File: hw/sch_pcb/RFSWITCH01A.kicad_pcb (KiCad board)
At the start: 2 copper layers, 40.1 x 40.1 mm, 43 parts, among them J1 HEADER_2x03_PARALLEL, J10 HEADER_2x01_PARALLEL, J2 SMA, J3 SMA, J4 HEADER_2x01_PARALLEL, J5 HEADER_2x01_PARALLEL, J6 HEADER_2x01_PARALLEL, J7 SMA, J8 SMA, J9 HEADER_2x01_PARALLEL, M1 HOLE, M2 HOLE, M3 HOLE, M4 HOLE, U1 TPS22945DCKR, U2 PE4259, U3 SPF5189Z, U4 PE4259

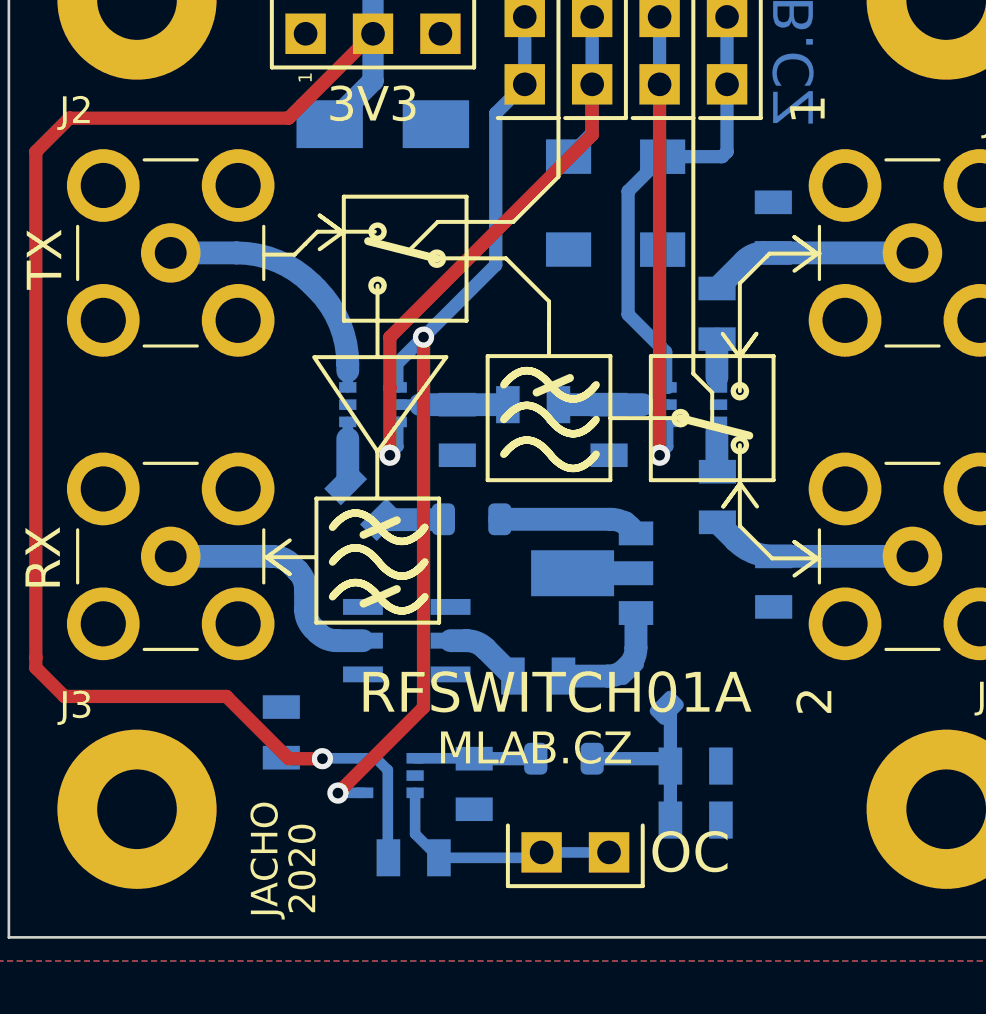
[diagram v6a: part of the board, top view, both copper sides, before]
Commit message: Diode, via, 3D model
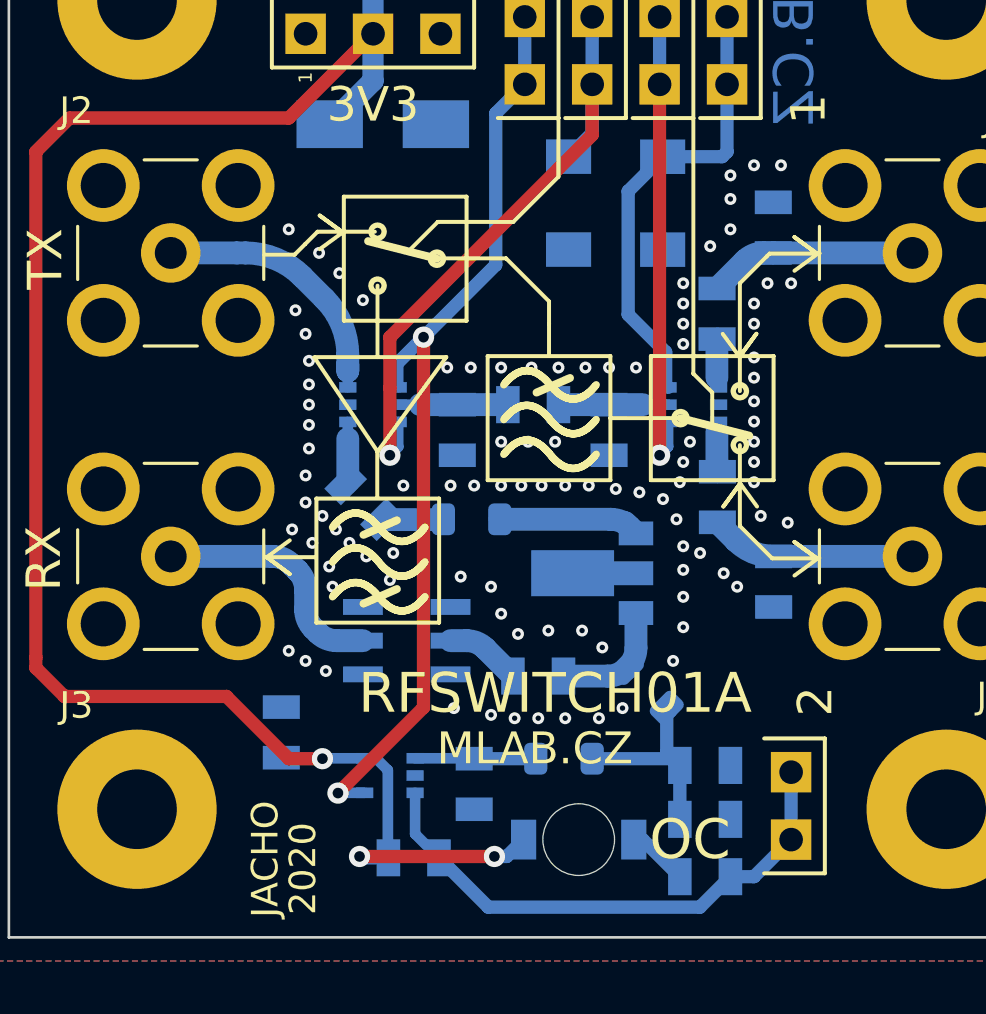
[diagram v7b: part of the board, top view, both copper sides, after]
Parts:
- added D4: RED, Mlab_D:LED_1206, B.Cu at (21.7, -3.94)
- added R6: 330R, Mlab_R:SMD-0805, B.Cu at (26.5, -2.54)
- moved J6 8.31 mm to (29.7, -5.21), turned to 90 degrees
- moved C4 0.36 mm to (26.5, -6.73)
- moved C3 0.36 mm to (26.5, -4.70)
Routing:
- net Net-(J6-Pad1): track 9.31 -> 21.0 mm
- net +3V3: track 74.8 -> 82.3 mm, vias 3 -> 5
- net Net-(D4-Pad1): track 0.00 -> 2.31 mm
- net Net-(C3-Pad1): track 7.35 -> 8.01 mm
- net GND: vias 0 -> 97

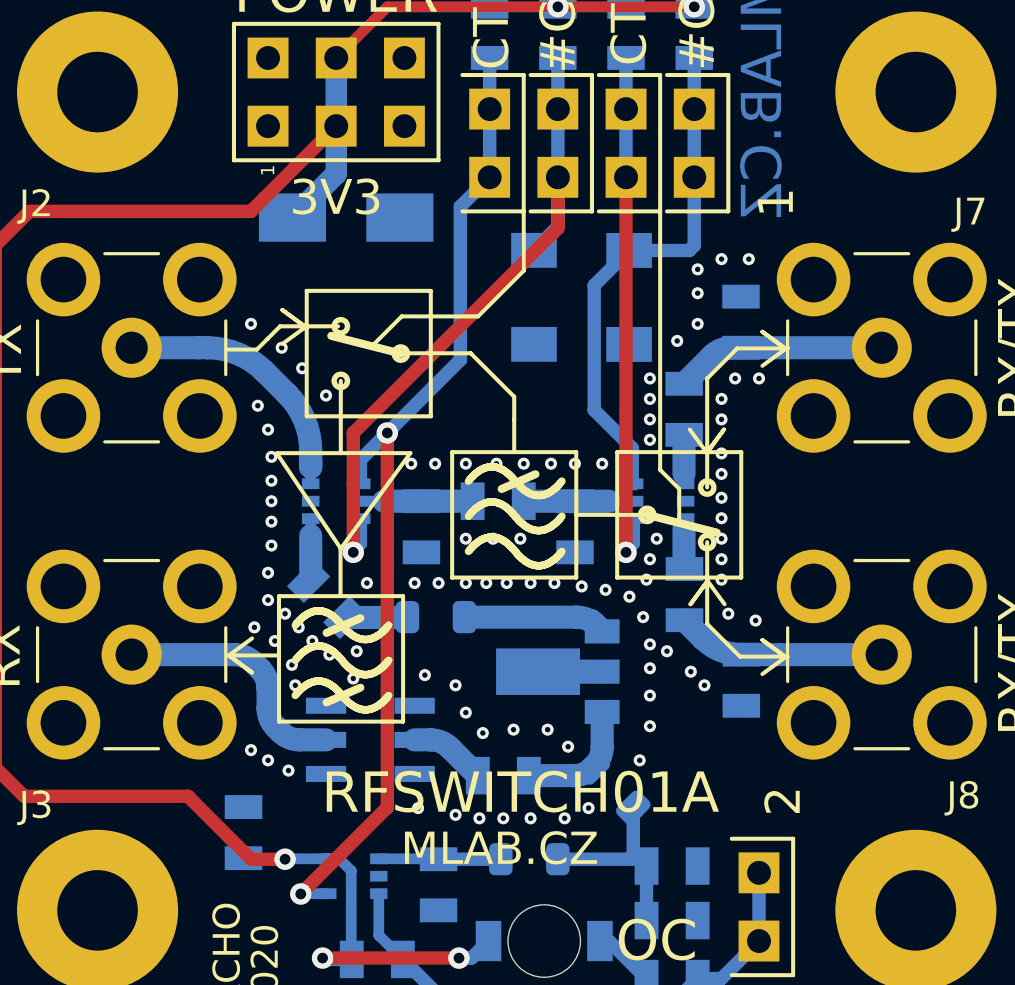
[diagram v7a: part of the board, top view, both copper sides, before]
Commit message: slight improvement of via shielding.
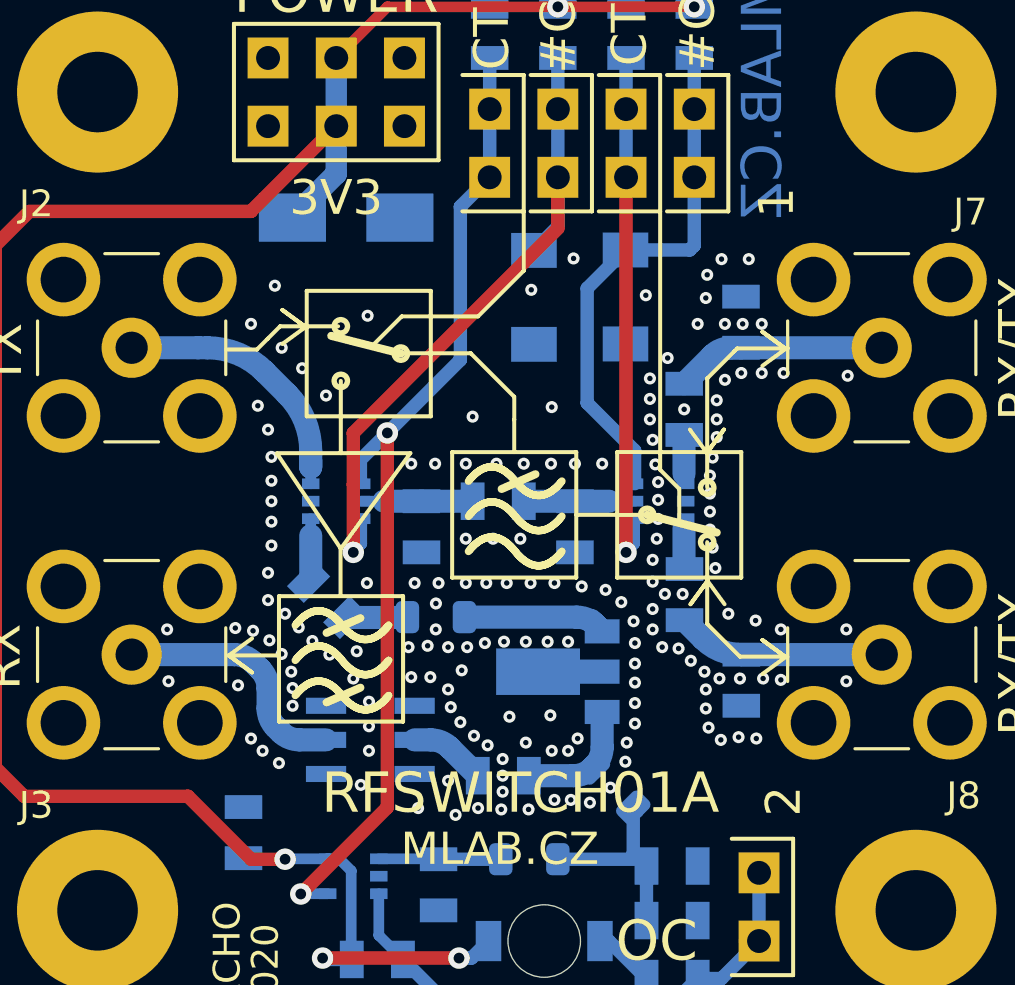
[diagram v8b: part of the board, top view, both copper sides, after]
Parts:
- moved D2 0.13 mm to (24.7, -27.9)
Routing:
- net GND: vias 97 -> 170
